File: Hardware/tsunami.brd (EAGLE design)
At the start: 74.9 x 73.7 mm, 155 parts, among them J1 VDC-IN, J10 TRIG2, J11 TRIG1, J12 USD-SDIO-SOCKET, J13 GND, J14 AUDIO I/O, J15 MIDI, J2 GND-IN, J3 DEBUG, J4 USB-MICROB", J5 CORTEX_DEBUGPTH, J6 3.3VA, J7 3.3V, J8 !PLAYING, J9 FTDI_DEVICE, Q1 2.5A/30V, U1 LM1117, U2 LM1117, U3 ATSAMS70NXXA-AN, U4 AK4618VQSFE-PACKAGE, U5 74AHC1G125, U6 6N138M, Y1 11.2896 MHz

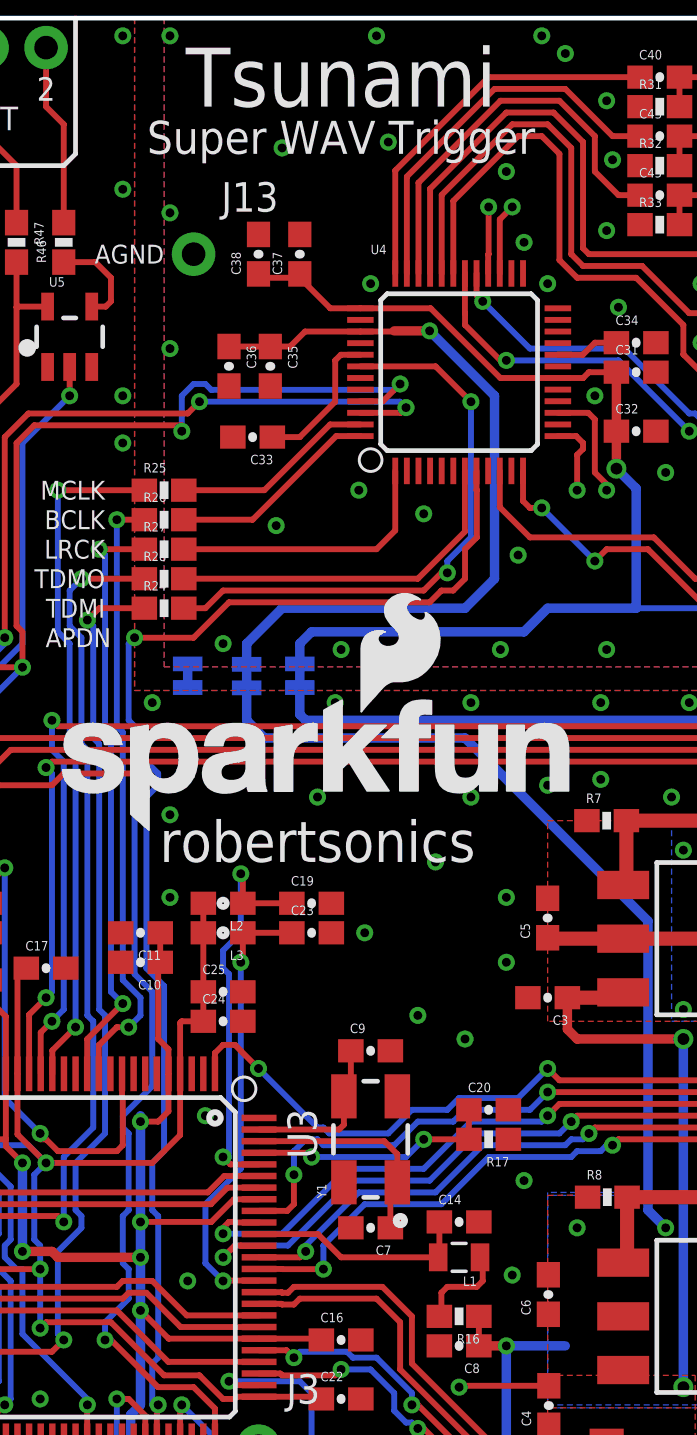
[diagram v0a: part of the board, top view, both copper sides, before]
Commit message: One more ground stitch via
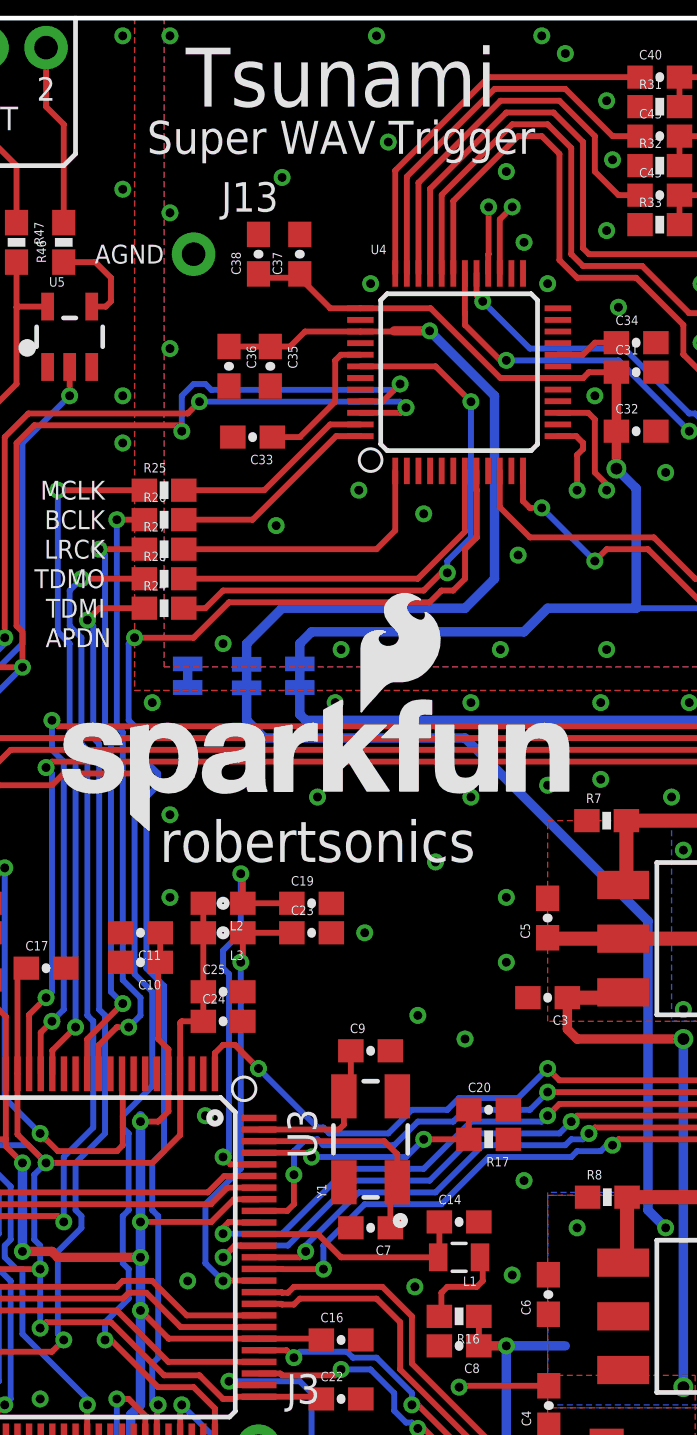
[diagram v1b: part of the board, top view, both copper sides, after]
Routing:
- net GND: vias 162 -> 163
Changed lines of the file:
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@@
 <setting verticaltext="up"/>
 </settings>
-<grid distance="0.01" unitdist="inch" unit="inch" style="lines" multiple="1" display="yes" altdistance="0.005" altunitdist="inch" altunit="inch"/>
+<grid distance="0.05" unitdist="inch" unit="inch" style="lines" multiple="1" display="yes" altdistance="0.005" altunitdist="inch" altunit="inch"/>
 <layers>
 <layer number="1" name="Top" color="4" fill="1" visible="yes" active="yes"/>
@@
 <via x="30.734" y="65.278" extent="1-16" drill="0.381"/>
 <via x="30.734" y="72.898" extent="1-16" drill="0.381"/>
-<via x="35.56" y="68.072" extent="1-16" drill="0.381"/>
+<via x="35.56" y="66.802" extent="1-16" drill="0.381"/>
 <via x="39.624" y="72.898" extent="1-16" drill="0.381"/>
 <via x="46.736" y="72.898" extent="1-16" drill="0.381"/>
@@
 <via x="9.652" y="16.002" extent="1-16" drill="0.381"/>
 <contactref element="J15" pad="4"/>
+<via x="41.275" y="19.05" extent="1-16" drill="0.381"/>
 </signal>
 <signal name="N$1">

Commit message: Updates from reviews.
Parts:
- added TP5: SWDIO/TMS, SparkFun-Passives:TP_15TH
- added TP6: SWCK/TCK, SparkFun-Passives:TP_15TH
- added TP7: TDO, SparkFun-Passives:TP_15TH
- added TP8: TDI, SparkFun-Passives:TP_15TH
- added TP9: NRESET, SparkFun-Passives:TP_15TH
- U3: value ATSAMS70NXXA-AN -> ATSAMS70N20A-AN
- moved C6 0.94 mm to (47.0, 17.8), turned to 180 degrees
- moved C5 0.90 mm to (46.9, 34.0), turned to 180 degrees
- moved C4 0.06 mm to (47.0, 14.0), turned to 180 degrees
- renumbered L2 to FB1, L3 to FB2, L4 to FB3
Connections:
- net 3.3V_A renamed VCCA
- net N$7 renamed VBUS
- new net SHIELD: J4.SHIELD1, J4.SHIELD2, J4.SHIELD3
- net NRESET: now also TP9.P$1
- net SWCLK/TCK: now also TP6.P$1
- net SWDIO/TMS: now also TP5.P$1
- net TDI: now also TP8.P$1
- net TDO: now also TP7.P$1
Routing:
- net VCCA: track 100.0 -> 77.7 mm
- net GND: track 4.90 -> 1.10 mm
- net 3.3V: track 313.8 -> 313.1 mm
- net TDI: track 11.0 -> 11.3 mm, vias 2 -> 1
- net TDO: vias 2 -> 1
- net NRESET: vias 2 -> 1
- added copper zone on layer 1, net SHIELD
- added copper zone on layer 16, net SHIELD

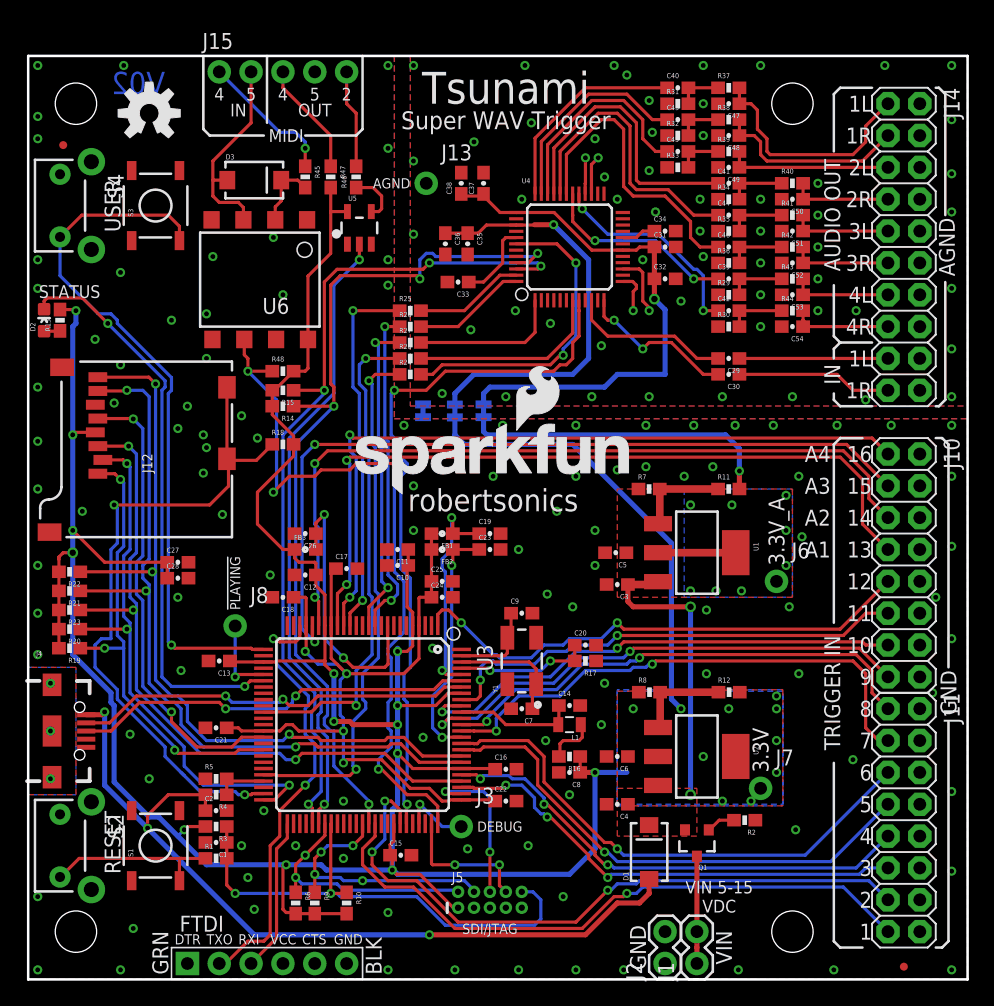
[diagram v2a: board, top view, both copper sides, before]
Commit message: Some checklist touchups
JTAG TP's placed on 50 mil grid.
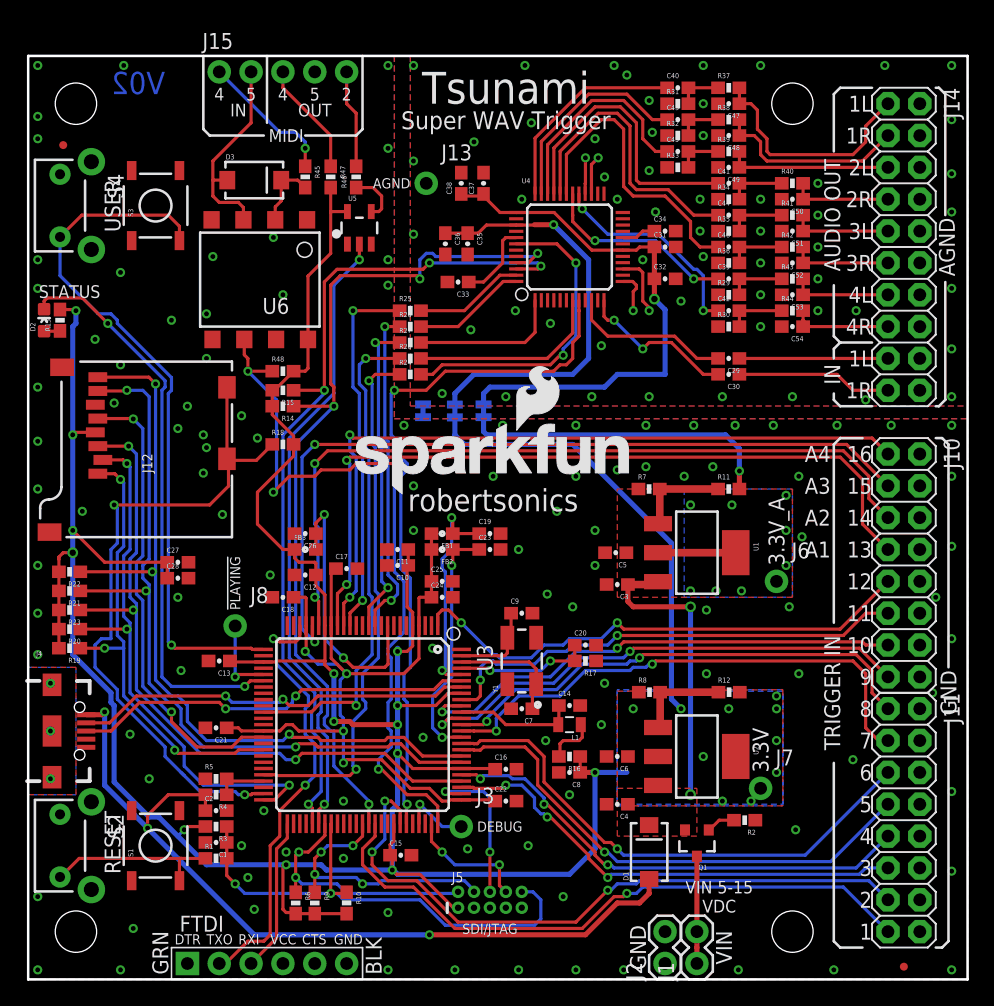
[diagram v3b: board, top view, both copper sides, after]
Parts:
- removed LOGO2, LOGO3: OSHW-LOGOM, SparkFun-Aesthetics:OSHW-LOGO-M
- moved TP8 1.44 mm to (33.0, 10.2)
- moved TP9 0.76 mm to (16.5, 7.62)
- moved TP5 0.57 mm to (21.6, 10.2)
- moved TP6 0.25 mm to (26.7, 7.62)
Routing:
- net TDI: track 11.3 -> 9.97 mm
- net SWDIO/TMS: track 19.9 -> 20.4 mm

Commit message: Addressing Eric's punch list.
See issue #2
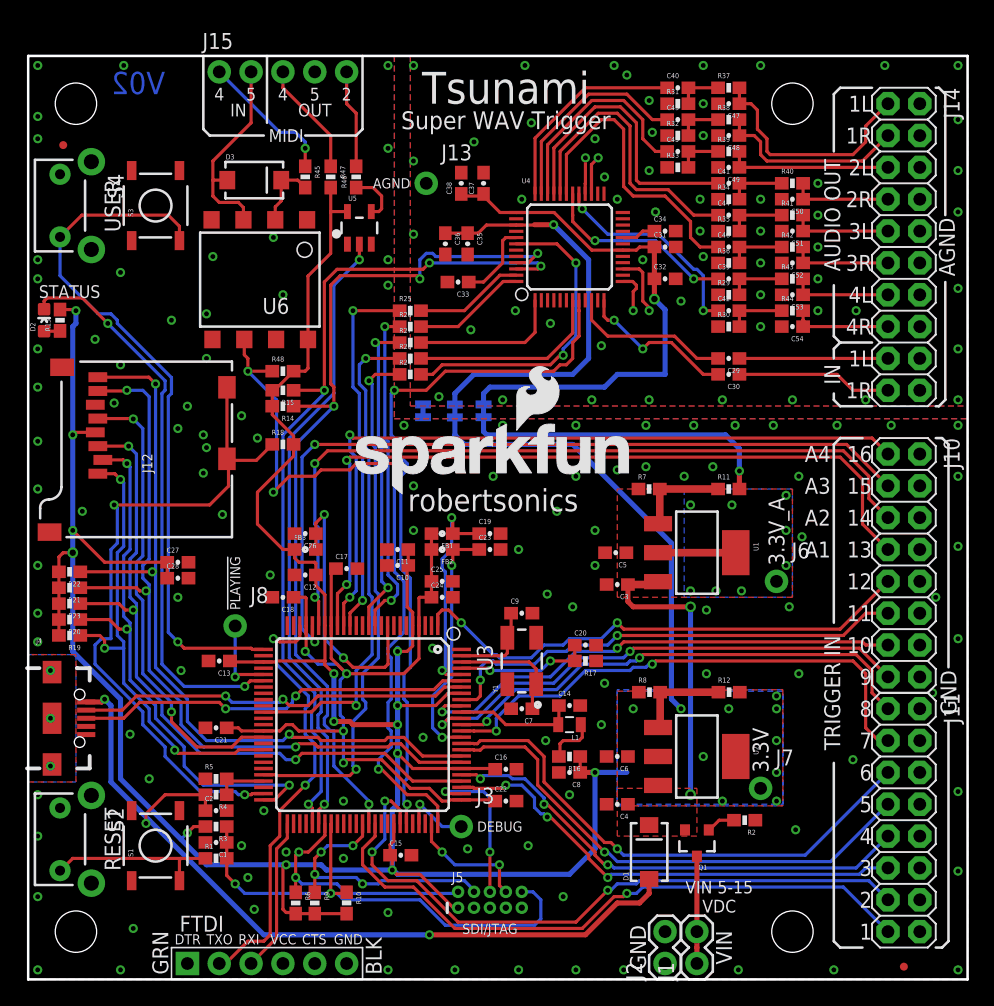
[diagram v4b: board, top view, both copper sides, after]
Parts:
- moved J4 1.02 mm to (1.91, 20.8)
- moved R19 1.02 mm to (3.30, 27.4)
- moved R20 0.76 mm to (3.30, 28.7)
- moved R23 0.51 mm to (3.30, 30.0)
- moved S2 0.51 mm to (2.54, 11.2)
- moved R21 0.25 mm to (3.30, 31.2)
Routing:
- net 3.3V: track 313.1 -> 311.4 mm
- net SDD2: track 36.6 -> 37.4 mm
- net VBUS: track 65.9 -> 66.6 mm
- net N$10: track 45.5 -> 44.9 mm
- net GND: vias 163 -> 166

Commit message: Updates for production.
Silkscreen touchups.
-all silk on back is right side up.
-some size & placement adjustments to labels.  Name is larger, some pad
labels are smaller.
-JTAG and DEBUG labels removed from both sides of board.
-Playing is active high, overbar deleted.

Only copper change is version number, rolled to ""V10."
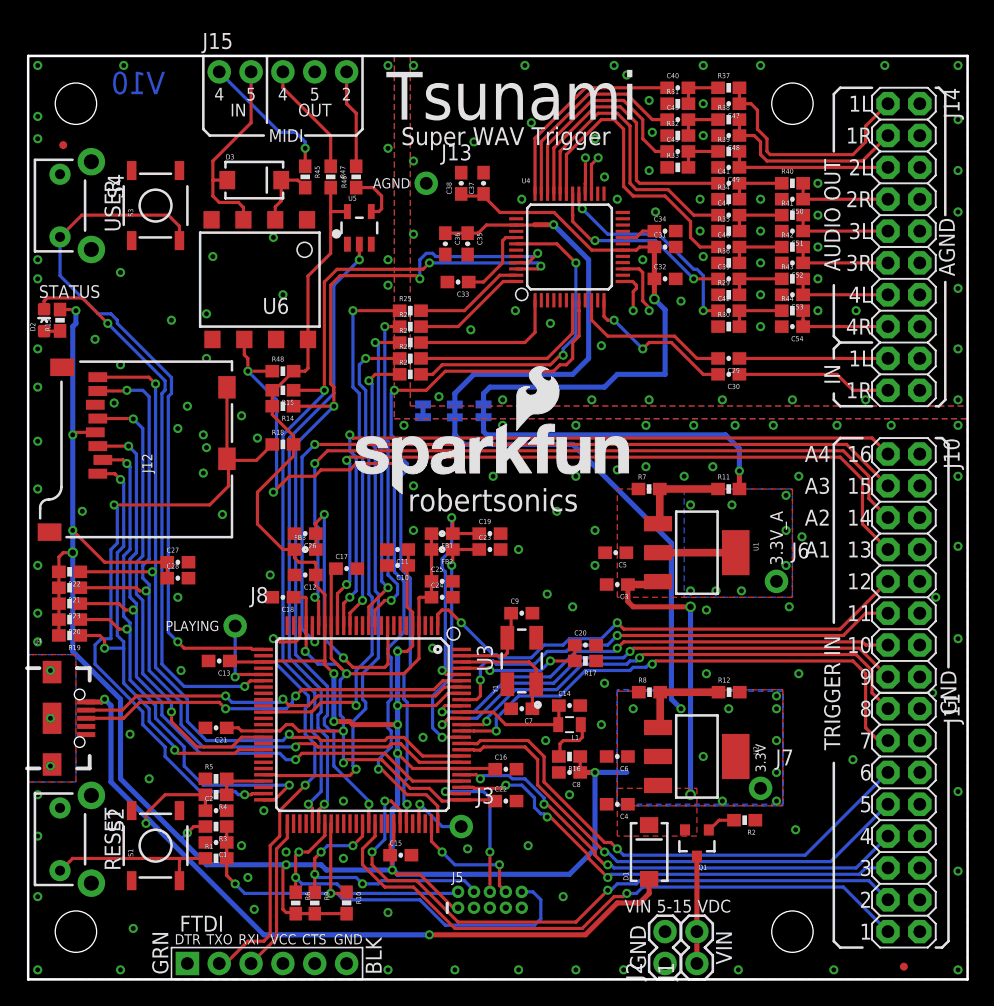
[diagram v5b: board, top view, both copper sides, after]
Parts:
- J8: value !PLAYING -> PLAYING
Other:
- board text added: "PLAYING"
- board text added: "V10"
- board text removed: "!PLAYING"
- board text removed: "SDI/JTAG"
- board text removed: "V02"
